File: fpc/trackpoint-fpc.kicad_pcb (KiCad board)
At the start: 2 copper layers, 30.9 x 22.1 mm, 2 parts

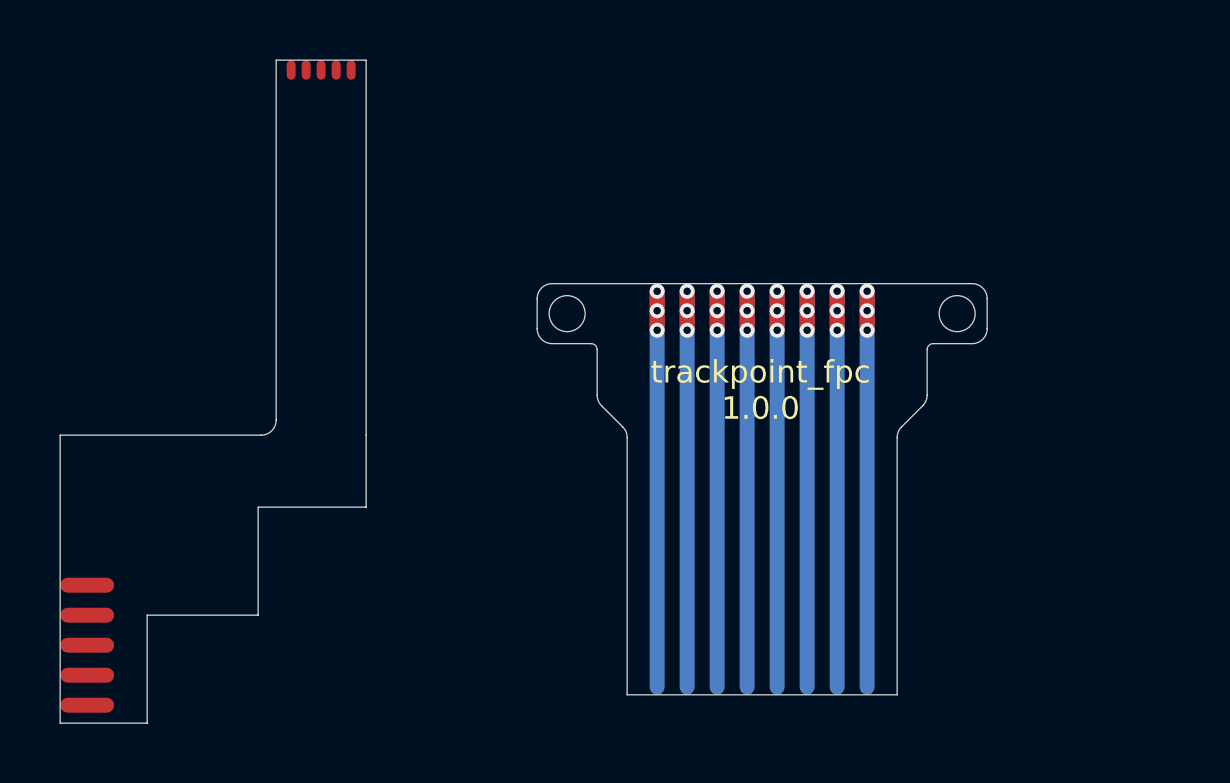
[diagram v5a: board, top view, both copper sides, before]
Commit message: Add FPC schematic, netlist, and add pad footprints to the board.
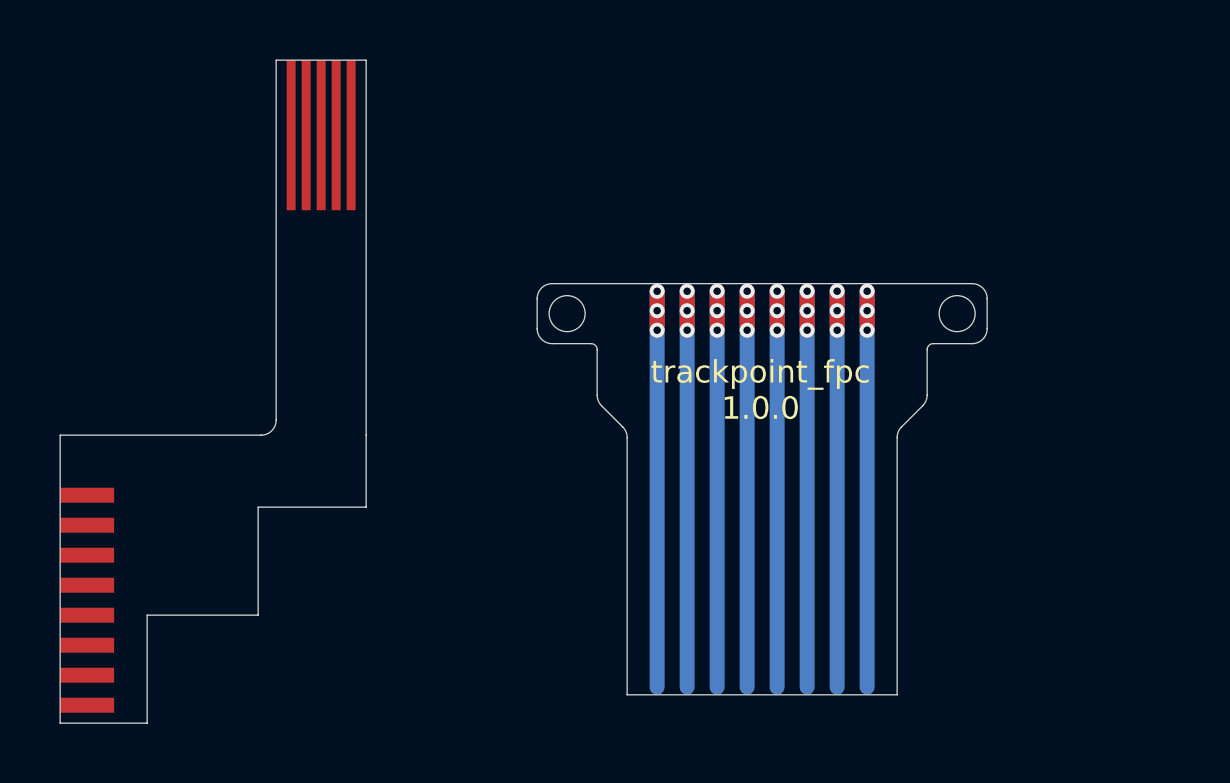
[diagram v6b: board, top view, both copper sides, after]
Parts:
- added P1: CONN_8, UGL:Trackpoint_FPC_8x1_pads, F.Cu at (190.5, 145.2)
- added P2: CONN_5, UGL:Trackpoint_FPC_5x0.5_pads, F.Cu at (198.3, 129.7)
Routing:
- net (no net): track 124.2 -> 116.0 mm
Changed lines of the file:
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@@
   (general
     (thickness 1.6)
-    (drawings 96)
-    (tracks 50)
+    (drawings 72)
+    (tracks 40)
     (zones 0)
-    (modules 2)
-    (nets 1)
+    (modules 4)
+    (nets 9)
   )
   (page A3)
@@
   )
   (setup
-    (last_trace_width 0.3)
+    (last_trace_width 0.5)
     (user_trace_width 0.3)
     (trace_clearance 0)
@@
   )
   (net 0 "")
+  (net 1 /VCC)
+  (net 2 /GND)
+  (net 3 /RESET)
+  (net 4 /CLK)
+  (net 5 /DATA)
+  (net 6 /RBTN)
+  (net 7 /MBTN)
+  (net 8 /LBTN)
   (net_class Default "This is the default net class."
     (clearance 0)
@@
     (diff_pair_width 0.5)
     (diff_pair_gap 0.25)
+    (add_net /CLK)
+    (add_net /DATA)
+    (add_net /GND)
+    (add_net /LBTN)
+    (add_net /MBTN)
+    (add_net /RBTN)
+    (add_net /RESET)
+    (add_net /VCC)
+  )
+  (module UGL:Trackpoint_FPC_5x0.5_pads (layer F.Cu)
+    (at 198.3 129.7)
+    (attr smd)
+    (fp_text reference P2 (at 0 3.65) (layer F.SilkS) hide
+      (effects (font (size 1 1) (thickness 0.15)))
+    )
+    (fp_text value CONN_5 (at 0 4.8) (layer F.Fab)
+      (effects (font (size 1 1) (thickness 0.15)))
+    )
+    (pad 1 smd rect (at -1 0) (size 0.3 5) (layers F.Cu F.Paste F.Mask)
+      (net 5 /DATA))
+    (pad 2 smd rect (at -0.5 0) (size 0.3 5) (layers F.Cu F.Paste F.Mask)
+      (net 4 /CLK))
+    (pad 3 smd rect (at 0 0) (size 0.3 5) (layers F.Cu F.Paste F.Mask)
+      (net 3 /RESET))
+    (pad 4 smd rect (at 0.5 0) (size 0.3 5) (layers F.Cu F.Paste F.Mask)
+      (net 2 /GND))
+    (pad 5 smd rect (at 1 0) (size 0.3 5) (layers F.Cu F.Paste F.Mask)
+      (net 1 /VCC))
   )
   (module UGL:hole_1.2000000476837158mm locked (layer F.Cu)
@@
     (pad "" np_thru_hole circle (at 0 0) (size 1.2 1.2) (drill 1.2) (layers *.Cu *.Mask)
       (clearance 0.00001))
+  )
+  (module UGL:Trackpoint_FPC_8x1_pads locked (layer F.Cu)
+    (at 190.5 145.2 270)
+    (attr smd)
+    (fp_text reference P1 (at 0 2.05 90) (layer F.SilkS) hide
+      (effects (font (size 1 1) (thickness 0.15)))
+    )
+    (fp_text value CONN_8 (at 0 3.2 90) (layer F.Fab)
+      (effects (font (size 1 1) (thickness 0.15)))
+    )
+    (pad 8 smd rect (at 3.5 0 270) (size 0.5 1.8) (layers F.Cu F.Paste F.Mask)
+      (net 1 /VCC))
+    (pad 7 smd rect (at 2.5 0 270) (size 0.5 1.8) (layers F.Cu F.Paste F.Mask)
+      (net 2 /GND))
+    (pad 6 smd rect (at 1.5 0 270) (size 0.5 1.8) (layers F.Cu F.Paste F.Mask)
+      (net 3 /RESET))
+    (pad 5 smd rect (at 0.5 0 270) (size 0.5 1.8) (layers F.Cu F.Paste F.Mask)
+      (net 4 /CLK))
+    (pad 4 smd rect (at -0.5 0 270) (size 0.5 1.8) (layers F.Cu F.Paste F.Mask)
+      (net 5 /DATA))
+    (pad 3 smd rect (at -1.5 0 270) (size 0.5 1.8) (layers F.Cu F.Paste F.Mask)
+      (net 6 /RBTN))
+    (pad 2 smd rect (at -2.5 0 270) (size 0.5 1.8) (layers F.Cu F.Paste F.Mask)
+      (net 7 /MBTN))
+    (pad 1 smd rect (at -3.5 0 270) (size 0.5 1.8) (layers F.Cu F.Paste F.Mask)
+      (net 8 /LBTN))
   )
   (gr_text "trackpoint_fpc\n1.0.0" (at 212.95 138.2) (layer F.SilkS)
@@
   (gr_arc (start 207.3 136.847262) (end 207.5 136.847257) (angle -89.98075418) (layer Edge.Cuts) (width 0.01))
   (gr_arc (start 218.7 136.847262) (end 218.7 136.647257) (angle -90.00839267) (layer Edge.Cuts) (width 0.01))
-  (gr_line (start 189.6 147.8975) (end 191.4 147.8975) (angle 90) (layer Cmts.User) (width 0.01))
-  (gr_line (start 191.4 147.4975) (end 189.6 147.4975) (angle 90) (layer Cmts.User) (width 0.01))
-  (gr_line (start 191.4 147.8975) (end 191.4 147.4975) (angle 90) (layer Cmts.User) (width 0.01))
-  (gr_line (start 189.6 145.8975) (end 191.4 145.8975) (angle 90) (layer Cmts.User) (width 0.01))
-  (gr_line (start 191.4 145.4975) (end 189.6 145.4975) (angle 90) (layer Cmts.User) (width 0.01))
-  (gr_line (start 191.4 145.8975) (end 191.4 145.4975) (angle 90) (layer Cmts.User) (width 0.01))
-  (gr_line (start 189.6 143.8975) (end 191.4 143.8975) (angle 90) (layer Cmts.User) (width 0.01))
-  (gr_line (start 191.4 143.4975) (end 189.6 143.4975) (angle 90) (layer Cmts.User) (width 0.01))
-  (gr_line (start 191.4 143.8975) (end 191.4 143.4975) (angle 90) (layer Cmts.User) (width 0.01))
-  (gr_line (start 189.6 141.8975) (end 191.4 141.8975) (angle 90) (layer Cmts.User) (width 0.01))
-  (gr_line (start 191.4 141.4975) (end 189.6 141.4975) (angle 90) (layer Cmts.User) (width 0.01))
-  (gr_line (start 191.4 141.8975) (end 191.4 141.4975) (angle 90) (layer Cmts.User) (width 0.01))
-  (gr_line (start 189.6 142.8975) (end 191.4 142.8975) (angle 90) (layer Cmts.User) (width 0.01))
-  (gr_line (start 191.4 142.4975) (end 189.6 142.4975) (angle 90) (layer Cmts.User) (width 0.01))
-  (gr_line (start 191.4 142.8975) (end 191.4 142.4975) (angle 90) (layer Cmts.User) (width 0.01))
-  (gr_line (start 189.6 144.8975) (end 191.4 144.8975) (angle 90) (layer Cmts.User) (width 0.01))
-  (gr_line (start 191.4 144.4975) (end 189.6 144.4975) (angle 90) (layer Cmts.User) (width 0.01))
-  (gr_line (start 191.4 144.8975) (end 191.4 144.4975) (angle 90) (layer Cmts.User) (width 0.01))
-  (gr_line (start 189.6 146.8975) (end 191.4 146.8975) (angle 90) (layer Cmts.User) (width 0.01))
-  (gr_line (start 191.4 146.4975) (end 189.6 146.4975) (angle 90) (layer Cmts.User) (width 0.01))
-  (gr_line (start 191.4 146.8975) (end 191.4 146.4975) (angle 90) (layer Cmts.User) (width 0.01))
-  (gr_line (start 189.6 148.8975) (end 191.4 148.8975) (angle 90) (layer Cmts.User) (width 0.01))
-  (gr_line (start 191.4 148.4975) (end 189.6 148.4975) (angle 90) (layer Cmts.User) (width 0.01))
-  (gr_line (start 191.4 148.8975) (end 191.4 148.4975) (angle 90) (layer Cmts.User) (width 0.01))
   (gr_line (start 199.8 127.1975) (end 199.8 139.6975) (angle 90) (layer Edge.Cuts) (width 0.01))
   (gr_line (start 196.8 127.1975) (end 196.8 139.1975) (angle 90) (layer Edge.Cuts) (width 0.01))
@@
   (segment (start 215.5 136.2) (end 215.5 134.902267) (width 0.5) (layer F.Cu) (net 0))
   (segment (start 216.5 136.2) (end 216.5 134.902267) (width 0.5) (layer F.Cu) (net 0))
-  (segment (start 191.15 144.7) (end 189.85501 144.7) (width 0.5) (layer F.Cu) (net 0))
-  (segment (start 191.15 145.7) (end 189.85501 145.7) (width 0.5) (layer F.Cu) (net 0))
-  (segment (start 191.15 146.7) (end 189.85501 146.7) (width 0.5) (layer F.Cu) (net 0))
-  (segment (start 191.15 147.7) (end 189.85501 147.7) (width 0.5) (layer F.Cu) (net 0))
-  (segment (start 191.15 148.7) (end 189.85501 148.7) (width 0.5) (layer F.Cu) (net 0))
-  (segment (start 198.3 127.7) (end 198.3 127.35251) (width 0.3) (layer F.Cu) (net 0))
-  (segment (start 199.3 127.7) (end 199.3 127.35251) (width 0.3) (layer F.Cu) (net 0))
-  (segment (start 197.8 127.7) (end 197.8 127.35251) (width 0.3) (layer F.Cu) (net 0))
-  (segment (start 197.3 127.7) (end 197.3 127.35251) (width 0.3) (layer F.Cu) (net 0))
-  (segment (start 198.8 127.7) (end 198.8 127.35251) (width 0.3) (layer F.Cu) (net 0))
 )

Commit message: Connect FPC pads.
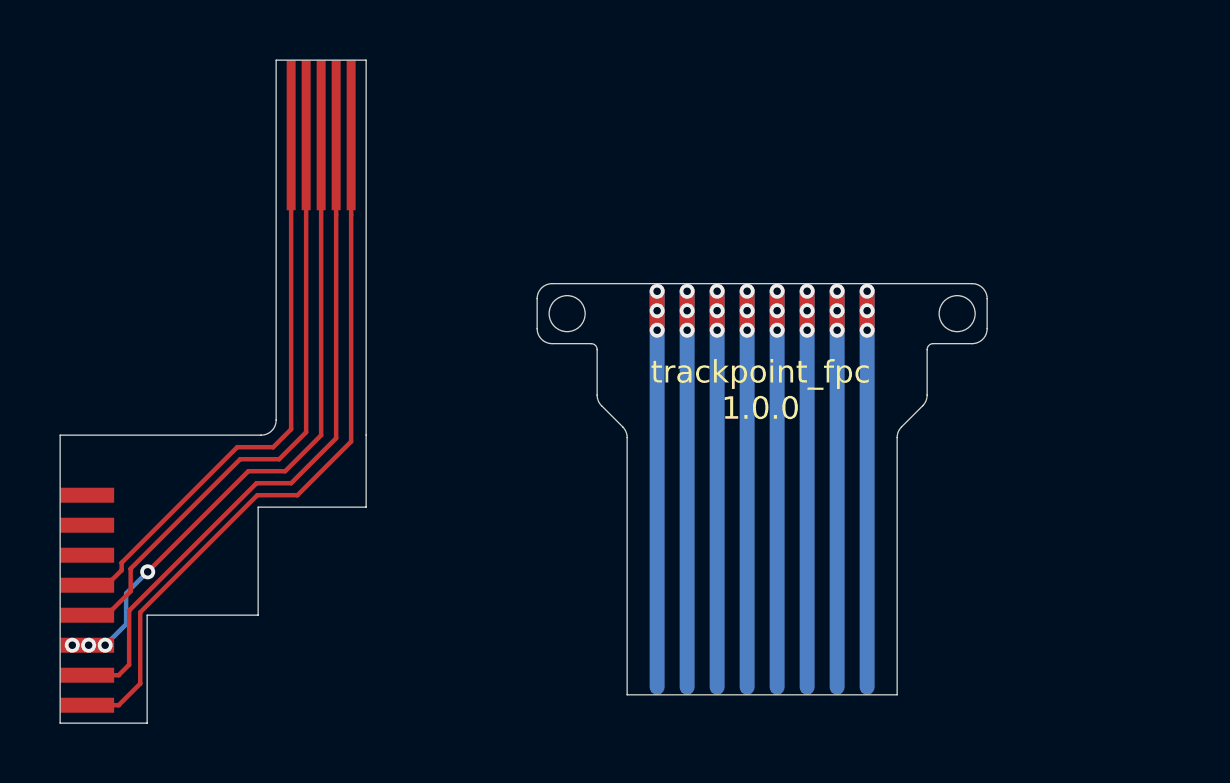
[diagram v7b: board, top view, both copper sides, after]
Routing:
- net /VCC: track 0.00 -> 24.8 mm
- net /GND: track 0.00 -> 23.5 mm
- net /RESET: track 0.00 -> 20.2 mm, vias 0 -> 4
- net /CLK: track 0.00 -> 18.9 mm
- net /DATA: track 0.00 -> 17.0 mm
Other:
- net class Default: clearance 0 -> 0.15; trace_width 0.5 -> 0.15
- rule trace_clearance: 0 -> 0.15
- rule trace_min: 0.254 -> 0.06
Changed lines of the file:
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@@
     (thickness 1.6)
     (drawings 72)
-    (tracks 40)
+    (tracks 87)
     (zones 0)
     (modules 4)
@@
   )
   (setup
-    (last_trace_width 0.5)
-    (user_trace_width 0.3)
-    (trace_clearance 0)
+    (last_trace_width 0.15)
+    (trace_clearance 0.15)
     (zone_clearance 0.508)
     (zone_45_only no)
-    (trace_min 0.254)
+    (trace_min 0.06)
     (via_size 0.5)
     (via_drill 0.25)
@@
   (net 8 /LBTN)
   (net_class Default "This is the default net class."
-    (clearance 0)
-    (trace_width 0.5)
+    (clearance 0.15)
+    (trace_width 0.15)
     (via_dia 0.5)
     (via_drill 0.25)
@@
   (segment (start 215.5 136.2) (end 215.5 134.902267) (width 0.5) (layer F.Cu) (net 0))
   (segment (start 216.5 136.2) (end 216.5 134.902267) (width 0.5) (layer F.Cu) (net 0))
+  (segment (start 190.5 148.7) (end 191.3 148.7) (width 0.2032) (layer F.Cu) (net 1))
+  (segment (start 199.3 139.912139) (end 199.3 132.35) (width 0.15) (layer F.Cu) (net 1))
+  (segment (start 197.512139 141.7) (end 199.3 139.912139) (width 0.15) (layer F.Cu) (net 1))
+  (segment (start 192.26999 145.602227) (end 196.172217 141.7) (width 0.15) (layer F.Cu) (net 1))
+  (segment (start 192.26999 147.98001) (end 192.26999 145.602227) (width 0.15) (layer F.Cu) (net 1))
+  (segment (start 196.172217 141.7) (end 197.512139 141.7) (width 0.15) (layer F.Cu) (net 1))
+  (segment (start 191.55 148.7) (end 192.26999 147.98001) (width 0.15) (layer F.Cu) (net 1))
+  (segment (start 199.3 132.35) (end 199.3 129.7) (width 0.15) (layer F.Cu) (net 1))
+  (segment (start 190.5 148.7) (end 191.55 148.7) (width 0.15) (layer F.Cu) (net 1))
+  (segment (start 190.5 147.7) (end 191.3 147.7) (width 0.2032) (layer F.Cu) (net 2))
+  (segment (start 198.8 132.35) (end 198.8 129.7) (width 0.15) (layer F.Cu) (net 2))
+  (segment (start 197.3 141.3) (end 198.8 139.8) (width 0.15) (layer F.Cu) (net 2))
+  (segment (start 190.5 147.7) (end 191.55 147.7) (width 0.15) (layer F.Cu) (net 2))
+  (segment (start 198.8 139.8) (end 198.8 132.35) (width 0.15) (layer F.Cu) (net 2))
+  (segment (start 191.899991 145.547947) (end 196.147938 141.3) (width 0.15) (layer F.Cu) (net 2))
+  (segment (start 191.55 147.7) (end 191.899991 147.350009) (width 0.15) (layer F.Cu) (net 2))
+  (segment (start 191.899991 147.350009) (end 191.899991 145.547947) (width 0.15) (layer F.Cu) (net 2))
+  (segment (start 196.147938 141.3) (end 197.3 141.3) (width 0.15) (layer F.Cu) (net 2))
+  (via (at 190.005 146.7) (size 0.5) (drill 0.25) (layers F.Cu B.Cu) (net 3))
+  (segment (start 190.5 146.7) (end 190.005 146.7) (width 0.15) (layer F.Cu) (net 3))
+  (via (at 190.55 146.7) (size 0.5) (drill 0.25) (layers F.Cu B.Cu) (net 3))
+  (segment (start 190.5 146.7) (end 190.6 146.7) (width 0.15) (layer F.Cu) (net 3))
+  (via (at 191.1 146.7) (size 0.5) (drill 0.25) (layers F.Cu B.Cu) (net 3))
+  (segment (start 190.5 146.7) (end 191.1 146.7) (width 0.15) (layer F.Cu) (net 3))
+  (via (at 192.517942 144.253825) (size 0.5) (drill 0.25) (layers F.Cu B.Cu) (net 3))
+  (segment (start 198.3 139.7) (end 198.3 131.4) (width 0.15) (layer F.Cu) (net 3))
+  (segment (start 197.1 140.9) (end 198.3 139.7) (width 0.15) (layer F.Cu) (net 3))
+  (segment (start 195.871767 140.9) (end 197.1 140.9) (width 0.15) (layer F.Cu) (net 3))
+  (segment (start 192.517942 144.253825) (end 195.871767 140.9) (width 0.15) (layer F.Cu) (net 3))
+  (segment (start 191.8 144.971767) (end 192.517942 144.253825) (width 0.15) (layer B.Cu) (net 3))
+  (segment (start 191.8 146) (end 191.8 144.971767) (width 0.15) (layer B.Cu) (net 3))
+  (segment (start 191.1 146.7) (end 191.8 146) (width 0.15) (layer B.Cu) (net 3))
+  (segment (start 190.5 145.7) (end 191.3 145.7) (width 0.15) (layer F.Cu) (net 4))
+  (segment (start 197.8 139.6) (end 197.8 131.8) (width 0.15) (layer F.Cu) (net 4))
+  (segment (start 196.9 140.5) (end 197.8 139.6) (width 0.15) (layer F.Cu) (net 4))
+  (segment (start 195.6 140.5) (end 196.9 140.5) (width 0.15) (layer F.Cu) (net 4))
+  (segment (start 191.950011 144.899989) (end 191.950011 144.149989) (width 0.15) (layer F.Cu) (net 4))
+  (segment (start 191.950011 144.149989) (end 195.6 140.5) (width 0.15) (layer F.Cu) (net 4))
+  (segment (start 191.15 145.7) (end 191.950011 144.899989) (width 0.15) (layer F.Cu) (net 4))
+  (segment (start 190.5 145.7) (end 191.15 145.7) (width 0.15) (layer F.Cu) (net 4))
+  (segment (start 197.3 139.5) (end 197.3 131.6) (width 0.15) (layer F.Cu) (net 5))
+  (segment (start 195.5 140.1) (end 196.7 140.1) (width 0.15) (layer F.Cu) (net 5))
+  (segment (start 191.65 143.95) (end 195.5 140.1) (width 0.15) (layer F.Cu) (net 5))
+  (segment (start 191.65 144.2) (end 191.65 143.95) (width 0.15) (layer F.Cu) (net 5))
+  (segment (start 191.15 144.7) (end 191.65 144.2) (width 0.15) (layer F.Cu) (net 5))
+  (segment (start 196.7 140.1) (end 197.3 139.5) (width 0.15) (layer F.Cu) (net 5))
+  (segment (start 190.5 144.7) (end 191.15 144.7) (width 0.15) (layer F.Cu) (net 5))
 )

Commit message: Add stiffener to the new FPC.
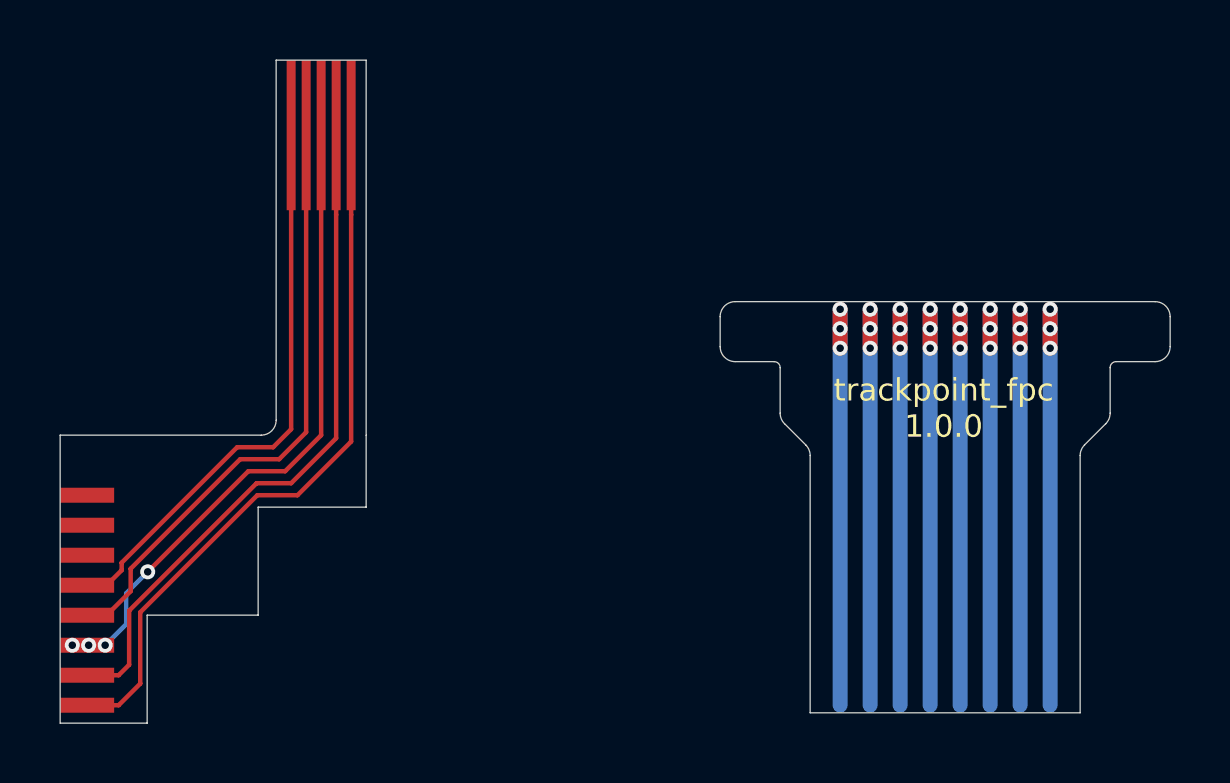
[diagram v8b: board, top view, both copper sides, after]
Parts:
- removed ? (x2): , UGL:hole_1.2000000476837158mm
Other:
- board size 30.9 x 22.1 mm -> 37 x 22.1 mm
